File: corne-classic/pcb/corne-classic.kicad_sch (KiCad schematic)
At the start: 87 parts, among them J1 MJ-4PP-9, J2 OLED, J3 LED, P1 i2c-pin, P2 i2c-pin, SW1 SW_PUSH, SW10 SW_PUSH, SW11 SW_PUSH, SW12 SW_PUSH, SW13 SW_PUSH, SW14 SW_PUSH, SW15 SW_PUSH, SW16 SW_PUSH, SW17 SW_PUSH, SW18 SW_PUSH, SW19 SW_PUSH, SW2 SW_PUSH, SW20 SW_PUSH, SW21 SW_PUSH, SW3 SW_PUSH, SW4 SW_PUSH, SW5 SW_PUSH, SW6 SW_PUSH, SW7 SW_PUSH, SW8 SW_PUSH, SW9 SW_PUSH, U1 ProMicro

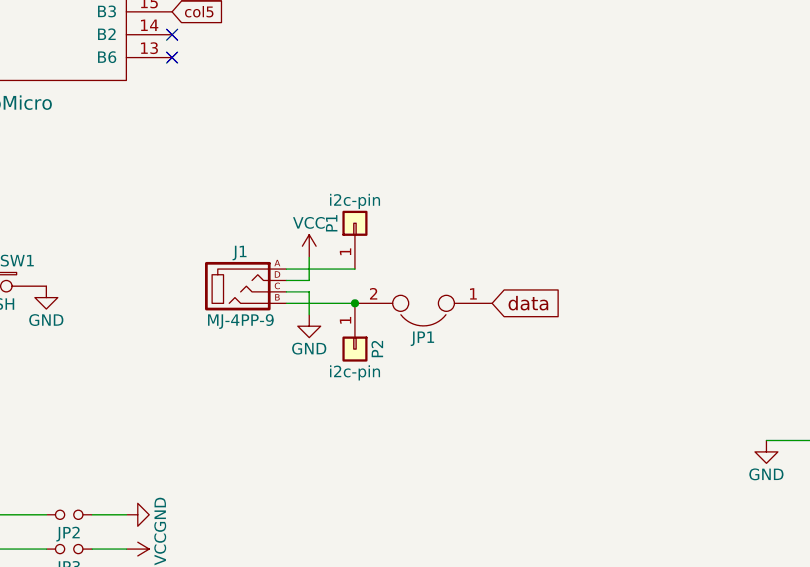
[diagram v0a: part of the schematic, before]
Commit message: added gateron low profile support
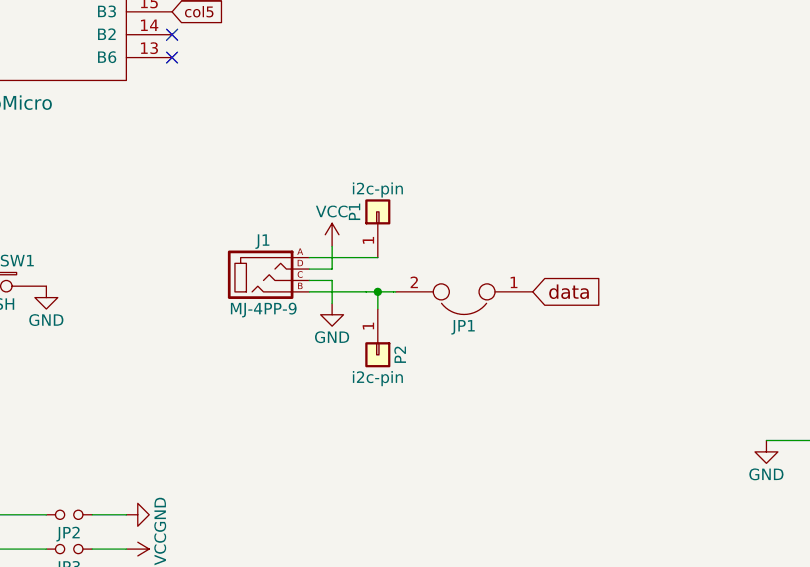
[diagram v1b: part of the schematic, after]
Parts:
- SW1, SW10, SW11, SW12, SW13, SW14, SW15, SW16, SW17, SW18, SW19, SW2, SW20, SW3, SW4, SW5, SW6, SW7, SW8, SW9: footprint kbd:MX_ALPS_PG1350_noLed -> gateron:Gateron_low_profile_noled_reversible_bighole
- SW21: footprint kbd:MX_ALPS_PG1350_noLed_1.75u -> gateron:Gateron_low_profile_noled_reversible_bighole
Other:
- moved on the sheet: J1, JP1, P1, P2
